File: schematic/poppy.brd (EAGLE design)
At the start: 31 x 51.9 mm, 18 parts, among them Q1 8MHz, U1 ATMEGA16U4TQFP44, U2 MBI5030GFSOP-24

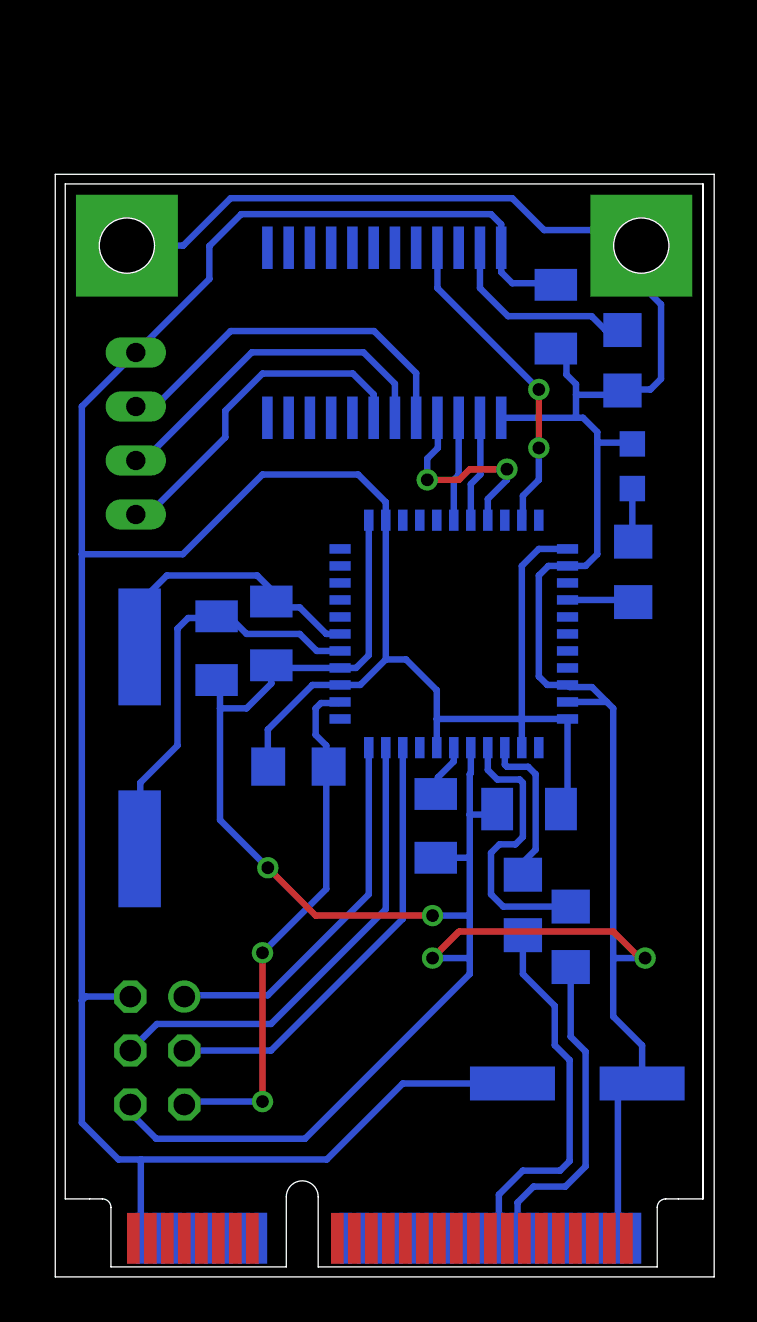
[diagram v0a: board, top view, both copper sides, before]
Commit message: added miniusb and second led
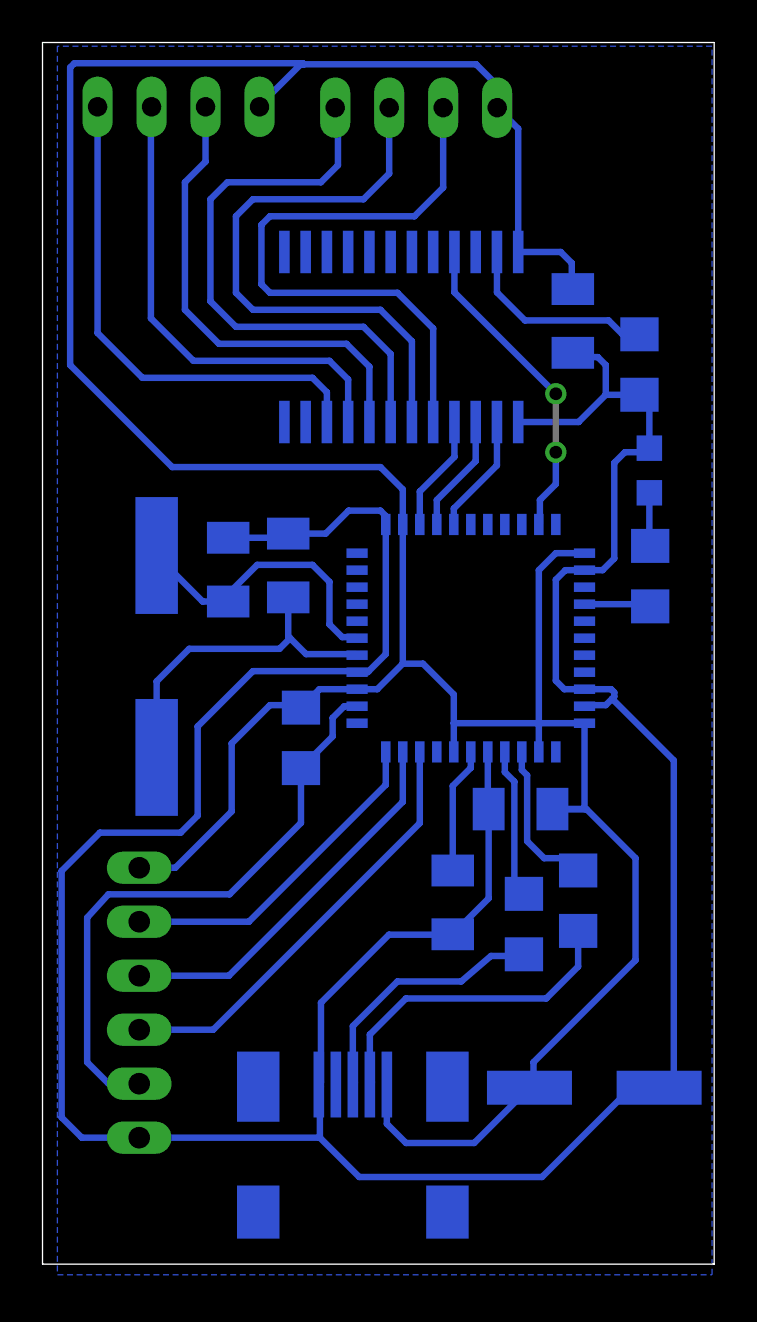
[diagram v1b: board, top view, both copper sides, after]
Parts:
- removed EDGE: (no value), mini-pci-e:FULL-MINI-PCI-E
- removed ISP: ISP1, con-lstb:MA03-2
- added LED3: CON-RGB-LED-EXT, _led-rgb:CON-RGB-LED-TH-EXT
- added SV1: (no value), con-lstb:MA06-1
- added X1: MINI-USB_SHIELD5P4-32005-400, con-cypressindustries:32005-400
- moved LED2 20.2 mm to (16.5, 54.5), turned to 90 degrees
- moved C4 5.15 mm to (10.5, 33.0), turned to 90 degrees
- moved Q1 4.37 mm to (4.27, 28.7)
- moved C5 3.69 mm to (18.2, 17.1)
- moved C3 3.62 mm to (7.63, 32.8), turned to 90 degrees
- moved R2 2.61 mm to (24.1, 17.2)
- moved R1 2.28 mm to (21.6, 16.1)
- moved R3 1.36 mm to (11.1, 24.9), turned to 90 degrees
- moved LED1 0.82 mm to (27.4, 37.4)
- moved R5 0.82 mm to (27.0, 42.4)
- moved U2 0.82 mm to (15.8, 43.8)
- moved C2 0.82 mm to (24.9, 8.40)
- moved U1 0.82 mm to (19.1, 29.6)
- moved C6 0.82 mm to (23.9, 44.5)
- moved R4 0.82 mm to (27.5, 32.5)
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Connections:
- removed net MOSI/DATA: ISP.4, U1.10
- new net MOSI: SV1.3, U1.10
- new net N$11: LED3.3.R, U2.8
- new net N$12: LED3.2.G, U2.9
- new net N$13: LED3.1.B, U2.10
- net D+: now also X1.3; no longer EDGE.38
- net D-: now also X1.2; no longer EDGE.36
- net DCLK: now also U1.26; no longer U1.28
- net GND: now also SV1.6, X1.5; no longer EDGE.50, EDGE.GND@1, EDGE.GND@2, ISP.6
- net LATCH: now also U1.25; no longer U1.30
- net MISO: now also SV1.2; no longer ISP.1
- net RESET: now also SV1.5; no longer ISP.5
- net SCK: now also SV1.4; no longer ISP.3
- net SDI: now also U1.27; no longer U1.29
- net VCC: now also LED3.4.VCC, SV1.1, X1.1; no longer EDGE.2, ISP.2
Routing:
- net N$13: track 0.00 -> 24.0 mm
- net GND: track 178.6 -> 154.7 mm, vias 4 -> 0
- net N$12: track 0.00 -> 22.4 mm
- net MOSI/DATA: track 22.4 -> 0.00 mm
- net N$11: track 0.00 -> 22.3 mm
- net MOSI: track 0.00 -> 18.1 mm
- net N$3: track 17.6 -> 29.2 mm
- net N$5: track 16.5 -> 27.8 mm
- net N$6: track 16.2 -> 26.9 mm
- net N$9: track 13.2 -> 7.00 mm
- net LATCH: track 9.87 -> 5.50 mm, vias 2 -> 0
- net RESET: track 24.9 -> 28.5 mm, vias 2 -> 0
- net XTAL2: track 19.7 -> 16.1 mm
- net N$4: track 2.53 -> 5.93 mm
- net D+: track 15.3 -> 12.3 mm
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- added copper zone on layer 16, net N$14
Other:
- board size 31 x 51.9 mm -> 31.6 x 57.5 mm

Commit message: reroute
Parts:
- moved LED1 12.7 mm to (27.8, 24.8), turned to 180 degrees
- moved R5 4.00 mm to (23.8, 44.8)
- moved C6 3.72 mm to (26.9, 42.3)
- moved R4 2.74 mm to (27.5, 29.7), turned to 90 degrees
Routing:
- net VCC: track 150.6 -> 157.9 mm
- net N$2: track 9.42 -> 5.19 mm
- net GND: track 154.7 -> 154.2 mm
